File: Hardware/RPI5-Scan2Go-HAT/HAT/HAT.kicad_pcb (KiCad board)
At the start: 2 copper layers, 65 x 56.5 mm, 33 parts, among them J1 RPi_GPIO, J10 Screw_Terminal_01x02, J11 Screw_Terminal_01x02, J12 Screw_Terminal_01x02, J13 Screw_Terminal_01x02, J14 Screw_Terminal_01x02, J15 Jack-DC 5V, J16 Screw_Terminal_01x02, J17 Screw_Terminal_01x02, J18 Screw_Terminal_01x02, J2 Screw_Terminal_01x03, J20 Screw_Terminal_01x05, J21 Screw_Terminal_01x06, J3 Conn_01x14_Socket, J4 Screw_Terminal_01x03, J5 Screw_Terminal_01x03, J6 Screw_Terminal_01x03, J7 Screw_Terminal_01x04, J8 Screw_Terminal_01x04, J9 Screw_Terminal_01x02, Q1 DMG2305UX, U1 Pico

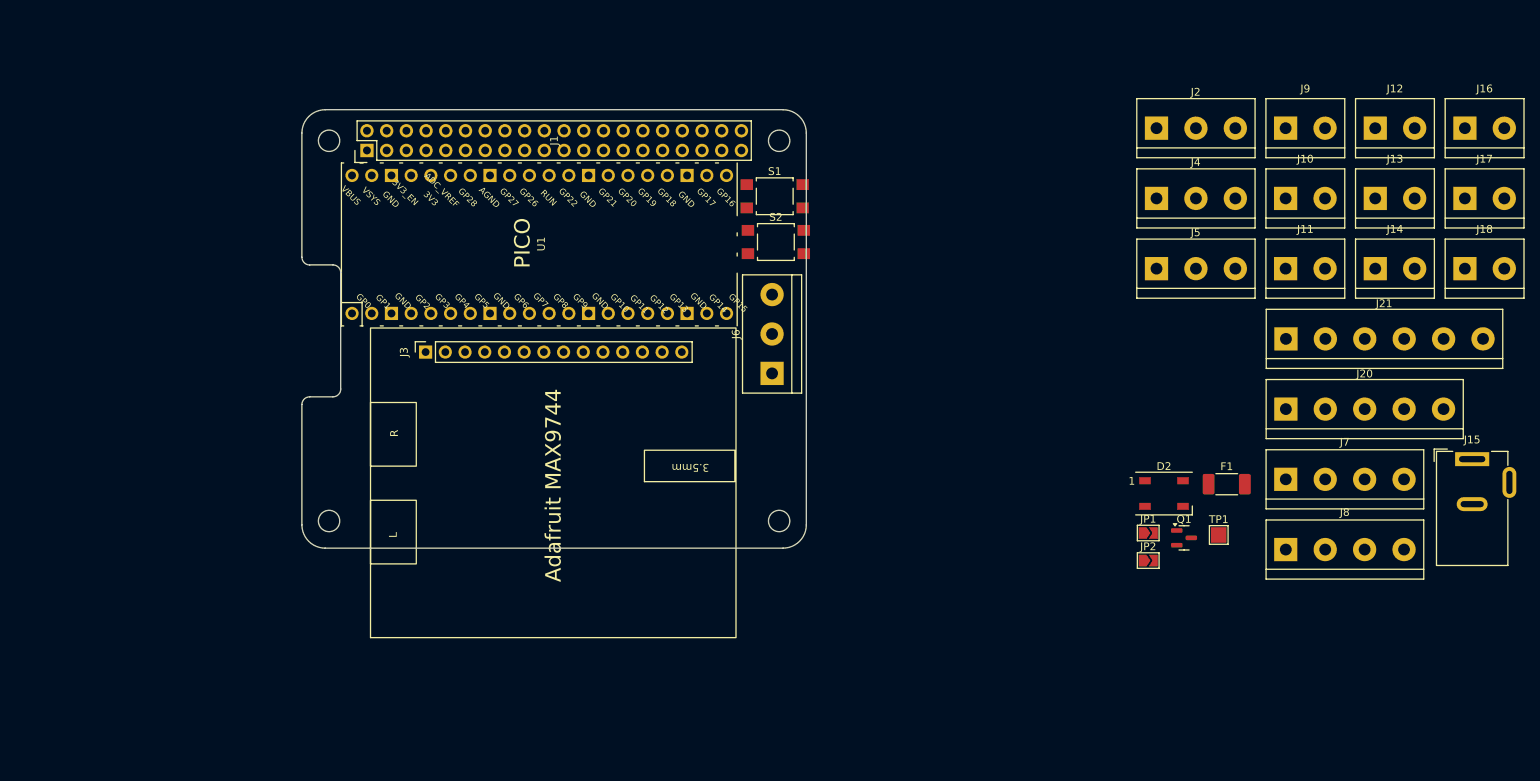
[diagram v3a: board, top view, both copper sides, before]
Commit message: changed requirements and pcb format
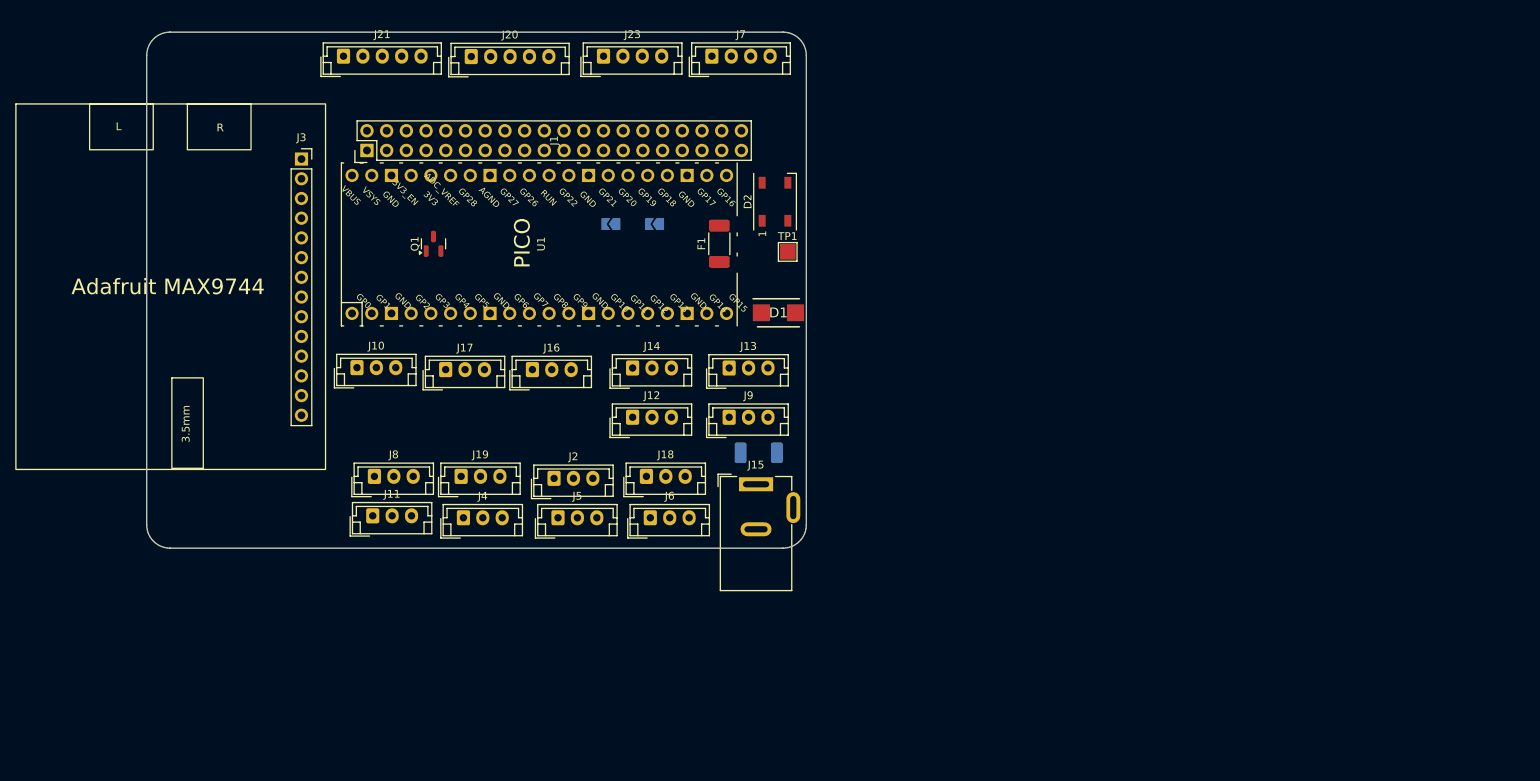
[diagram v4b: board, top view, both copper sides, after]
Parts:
- removed ? (x4): , RPi_Hat:RPi_Hat_Mounting_Hole
- removed S1, S2: MOMENTARY-SWITCH-SPST-2-SMD-5.2MM, Button_Switch_SMD:SW_SPST_TL3305B
- added D1: SMBJ26A, SamacSys_Parts:DIOM5436X261N, F.Cu at (168.9, 90.2)
- added F1: 6A, Fuse:Fuse_2010_5025Metric_Pad1.52x2.65mm_HandSolder, B.Cu at (166.4, 108.2)
- added J19: Conn_01x02_Socket, Connector_JST:JST_EH_B3B-EH-A_1x03_P2.50mm_Vertical, F.Cu at (128.0, 111.3)
- added J23: Conn_01x04_Socket, Connector_JST:JST_EH_B4B-EH-A_1x04_P2.50mm_Vertical, F.Cu at (146.4, 57.1)
- J10, J11, J12, J13, J14, J16, J17, J18, J9: value Screw_Terminal_01x02 -> Conn_01x02_Socket; footprint TerminalBlock:TerminalBlock_bornier-2_P5.08mm -> Connector_JST:JST_EH_B3B-EH-A_1x03_P2.50mm_Vertical
- J2, J4, J5, J6: value Screw_Terminal_01x03 -> Conn_01x03_Socket; footprint TerminalBlock:TerminalBlock_bornier-3_P5.08mm -> Connector_JST:JST_EH_B3B-EH-A_1x03_P2.50mm_Vertical
- J20: value Screw_Terminal_01x05 -> Conn_01x05_Socket; footprint TerminalBlock:TerminalBlock_bornier-5_P5.08mm -> Connector_JST:JST_EH_B5B-EH-A_1x05_P2.50mm_Vertical
- J21: value Screw_Terminal_01x06 -> Conn_01x05_Socket; footprint TerminalBlock:TerminalBlock_bornier-6_P5.08mm -> Connector_JST:JST_EH_B5B-EH-A_1x05_P2.50mm_Vertical
- J7: value Screw_Terminal_01x04 -> Conn_01x04_Socket; footprint TerminalBlock:TerminalBlock_bornier-4_P5.08mm -> Connector_JST:JST_EH_B4B-EH-A_1x04_P2.50mm_Vertical
- J8: value Screw_Terminal_01x04 -> Conn_01x02_Socket; footprint TerminalBlock:TerminalBlock_bornier-4_P5.08mm -> Connector_JST:JST_EH_B3B-EH-A_1x03_P2.50mm_Vertical
- JP1, JP2: moved to B.Cu
- moved J17 133.2 mm to (126.0, 97.5)
- moved J21 126.8 mm to (112.9, 57.1)
- moved J16 124.1 mm to (137.2, 97.5)
- moved J11 121.9 mm to (116.6, 116.3)
- moved J10 121.6 mm to (114.6, 97.2)
- moved J8 117.8 mm to (116.8, 111.3)
- moved J20 114.4 mm to (129.3, 57.1)
- moved J18 108.8 mm to (151.9, 111.3)
- moved Q1 103.9 mm to (124.5, 81.3), turned to 90 degrees
- moved J12 102.7 mm to (150.1, 103.6)
- moved J4 98.3 mm to (128.3, 116.6)
- moved J14 96.6 mm to (150.1, 97.3)
- moved J15 92.3 mm to (166.0, 112.3)
- moved J7 91.9 mm to (160.3, 57.1)
- moved J2 89.8 mm to (140.0, 111.5)
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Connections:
- J1 pad 16: unconnected-(J1-BCM23-Pad16) -> /PICORST
- J8 pad 1: GND -> /PICORST
- J8 pad 2: Net-(J8-Pin_2) -> GND
- J8 pad 3: Net-(J8-Pin_3) -> (no net)
- U1 pad 1: Net-(J8-Pin_3) -> Net-(J23-Pin_3)
- U1 pad 2: Net-(J8-Pin_2) -> Net-(J23-Pin_2)
- U1 pad 30: Net-(U1-RUN) -> /PICORST
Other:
- board size 65 x 56.5 mm -> 85 x 66.5 mm

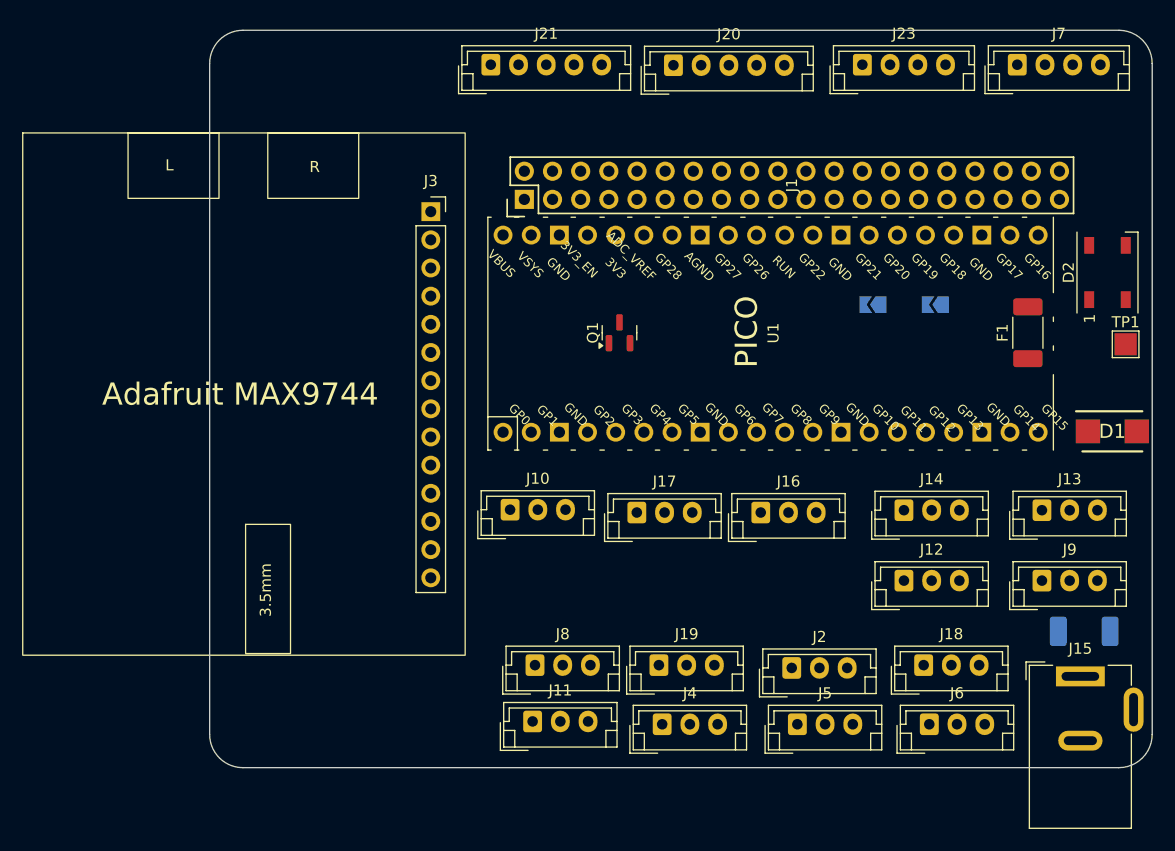
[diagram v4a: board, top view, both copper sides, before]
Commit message: added 3d models to design
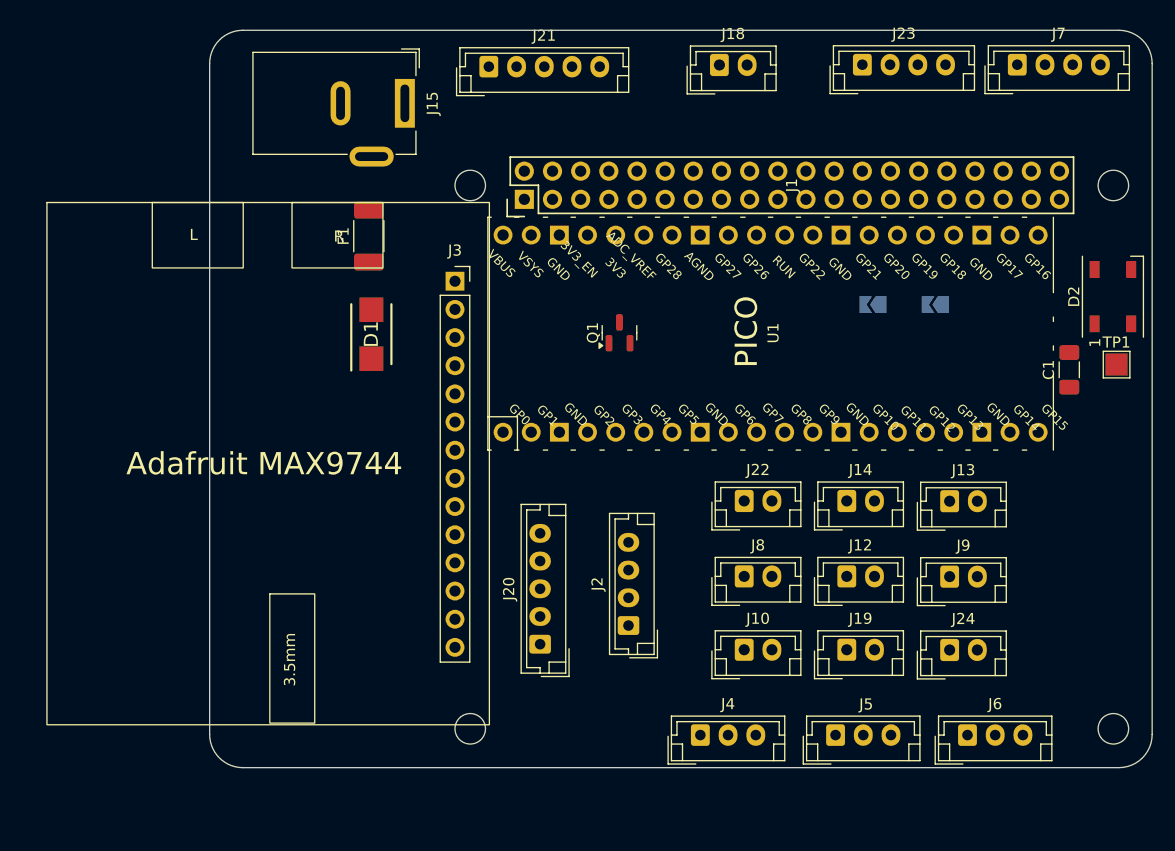
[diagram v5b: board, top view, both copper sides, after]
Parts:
- removed the F1 at (166.4, 108.2)
- removed J11, J16, J17: Conn_01x02_Socket, Connector_JST:JST_EH_B3B-EH-A_1x03_P2.50mm_Vertical
- added ?: , RPi_Hat:RPi_Hat_Mounting_Hole, F.Cu at (169.0, 117.0)
- added ?: , RPi_Hat:RPi_Hat_Mounting_Hole, F.Cu at (111.0, 117.0)
- added ?: , RPi_Hat:RPi_Hat_Mounting_Hole, F.Cu at (111.0, 68.0)
- added ?: , RPi_Hat:RPi_Hat_Mounting_Hole, F.Cu at (169.0, 68.0)
- added C1: 0.1uF, Capacitor_SMD:C_1206_3216Metric_Pad1.33x1.80mm_HandSolder, F.Cu at (165.0, 84.6)
- added J22: Conn_01x02_Socket, Connector_JST:JST_EH_B2B-EH-A_1x02_P2.50mm_Vertical, F.Cu at (135.7, 96.4)
- added J24: Conn_01x02_Socket, Connector_JST:JST_EH_B2B-EH-A_1x02_P2.50mm_Vertical, F.Cu at (154.2, 109.9)
- J10, J12, J13, J14, J18, J19, J8, J9: footprint Connector_JST:JST_EH_B3B-EH-A_1x03_P2.50mm_Vertical -> Connector_JST:JST_EH_B2B-EH-A_1x02_P2.50mm_Vertical
- J2: value Conn_01x03_Socket -> Conn_01x04_Socket; footprint Connector_JST:JST_EH_B3B-EH-A_1x03_P2.50mm_Vertical -> Connector_JST:JST_EH_B4B-EH-A_1x04_P2.50mm_Vertical
- moved J15 79.9 mm to (105.1, 60.6), turned to -90 degrees
- moved D1 67.4 mm to (102.1, 81.4), turned to 90 degrees
- moved F1 60.1 mm to (101.9, 72.6)
- moved J18 57.2 mm to (133.5, 57.1)
- moved J20 53.6 mm to (117.3, 109.4), turned to 90 degrees
- moved J10 24.6 mm to (135.7, 109.9)
- moved J8 20.5 mm to (135.7, 103.3)
- moved J19 17.0 mm to (145.0, 109.9)
- moved J2 15.2 mm to (125.3, 107.7), turned to 90 degrees
- moved J13 8.37 mm to (154.2, 96.5)
- moved J9 8.33 mm to (154.2, 103.3)
- moved J3 6.64 mm to (109.6, 76.6)
- moved J14 5.22 mm to (145.0, 96.4)
- moved J12 5.17 mm to (145.0, 103.3)
- moved J4 3.58 mm to (131.8, 117.6)
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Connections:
- U1 pad 10: Net-(J2-Pin_3) -> Net-(J10-Pin_2)
- U1 pad 11: Net-(J2-Pin_2) -> Net-(J22-Pin_2)
- U1 pad 12: Net-(J2-Pin_1) -> Net-(J24-Pin_2)
- U1 pad 21: Net-(J10-Pin_2) -> Net-(J2-Pin_4)
- U1 pad 22: Net-(J11-Pin_2) -> Net-(J2-Pin_3)
- U1 pad 24: Net-(J16-Pin_2) -> Net-(J2-Pin_2)
- U1 pad 25: Net-(J17-Pin_2) -> Net-(J2-Pin_1)

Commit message: improved layout
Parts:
- added G***: LOGO, LOGO, F.Cu at (119.7, 73.9)
- moved J18 88.5 mm to (130.6, 145.6)
- moved J23 80.6 mm to (140.6, 137.5)
- moved J21 78.1 mm to (122.9, 134.7)
- moved J7 77.0 mm to (140.2, 131.4)
- moved J15 74.4 mm to (113.2, 134.5), turned to 0 degrees
- moved D1 67.4 mm to (162.3, 111.8), turned to 180 degrees
- moved F1 64.9 mm to (153.4, 112.0), turned to 180 degrees
- moved J3 63.4 mm to (171.7, 89.6), turned to -90 degrees
- moved J24 34.2 mm to (174.6, 137.3)
- moved J10 34.2 mm to (156.1, 137.3)
- moved J13 34.2 mm to (174.6, 123.9)
- moved J19 34.2 mm to (165.4, 137.3)
- moved J12 34.2 mm to (165.4, 130.7)
- moved J14 34.2 mm to (165.4, 123.9)
- moved J22 34.2 mm to (156.1, 123.9)
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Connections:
- J21 pad 4: Net-(J21-Pin_4) -> (no net)
- U1 pad 36: Net-(J21-Pin_4) -> (no net)
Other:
- board size 85 x 66.5 mm -> 76 x 96.5 mm
- board text added: "Name: Raspberry Pi HAT Project: Scan2Go Date: 13-05-24 Version: 0.1"

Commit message: started routing
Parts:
- JP1, JP2: moved to F.Cu
- moved D2 67.0 mm to (113.5, 116.9), turned to 180 degrees
- moved C1 65.0 mm to (110.6, 110.0)
- moved TP1 65.0 mm to (114.9, 109.5)
- moved D1 52.5 mm to (112.8, 129.5)
- moved F1 42.2 mm to (113.0, 124.1)
- moved JP1 29.5 mm to (144.7, 84.0), turned to 0 degrees
- moved JP2 29.2 mm to (139.4, 84.0), turned to 0 degrees
- moved J18 25.2 mm to (142.3, 123.2)
- moved Q1 16.6 mm to (120.3, 117.0)
- moved J2 16.2 mm to (124.4, 123.5)
- moved J21 2.63 mm to (122.9, 137.3)
- moved J20 1.73 mm to (122.9, 130.1)
- moved J15 0.76 mm to (112.5, 134.8)
- moved J23 0.66 mm to (140.2, 137.0)
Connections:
- J21 pad 4: (no net) -> Net-(J21-Pin_4)
- U1 pad 36: (no net) -> Net-(J21-Pin_4)
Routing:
- net Net-(J20-Pin_5): track 0.00 -> 35.8 mm
- net Net-(J1-BCM12_PWM0): track 0.00 -> 25.8 mm
- net Net-(J1-BCM17): track 0.00 -> 21.8 mm
- net Net-(J1-BCM18_PCM_C): track 0.00 -> 11.0 mm
- net /PICORST: track 0.00 -> 9.05 mm
- net GND: track 0.00 -> 7.41 mm
- net Net-(J3-LIN): track 0.00 -> 6.82 mm
- net Net-(J3-RIN): track 0.00 -> 5.61 mm
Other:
- board text removed: "GND"
- board text removed: "GP0"
- board text removed: "GP1"
- board text removed: "GP10"
- board text removed: "GP11"
- board text removed: "GP12"
- board text removed: "GP13"
- board text removed: "GP14"
- board text removed: "GP15"
- board text removed: "GP2"
- board text removed: "GP3"
- board text removed: "GP4"
- board text removed: "GP5"
- board text removed: "GP6"
- board text removed: "GP7"
- board text removed: "GP8"
- board text removed: "GP9"
